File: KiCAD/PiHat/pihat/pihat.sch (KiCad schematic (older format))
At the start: 13 parts, among them J1 Conn_01x03, J2 Conn_01x03, P1 Conn_02x20_Odd_Even, Q1 BSS138, Q2 BSS138

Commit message: compacted servo design
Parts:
- J1, J2: symbol Connector_Generic:Conn_01x03 -> pihat-rescue:Conn_01x03-Connector_Generic
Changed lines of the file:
@@
 EESchema Schematic File Version 4
-LIBS:pihat-cache
 EELAYER 30 0
 EELAYER END
@@
 Connection ~ 7000 3550
 Text GLabel 7450 4450 2    50   Input ~ 0
-GPIO_17
+GPIO_2
 Text Label 8450 3600 2    50   ~ 0
 PAN_SERVO_PIN
@@
 	7000 3550 7450 3550
 Text GLabel 7450 3550 2    50   Input ~ 0
-GPIO_27
+GPIO_3
 Wire Wire Line
 	6050 4450 7450 4450
@@
 GPIO_27
 $Comp
-L Connector_Generic:Conn_01x03 J1
+L pihat-rescue:Conn_01x03-Connector_Generic J1
 U 1 1 5E51AE8D
 P 5300 2550
@@
 Connection ~ 5400 4450
 $Comp
-L Connector_Generic:Conn_01x03 J2
+L pihat-rescue:Conn_01x03-Connector_Generic J2
 U 1 1 5E545433
 P 6250 2550

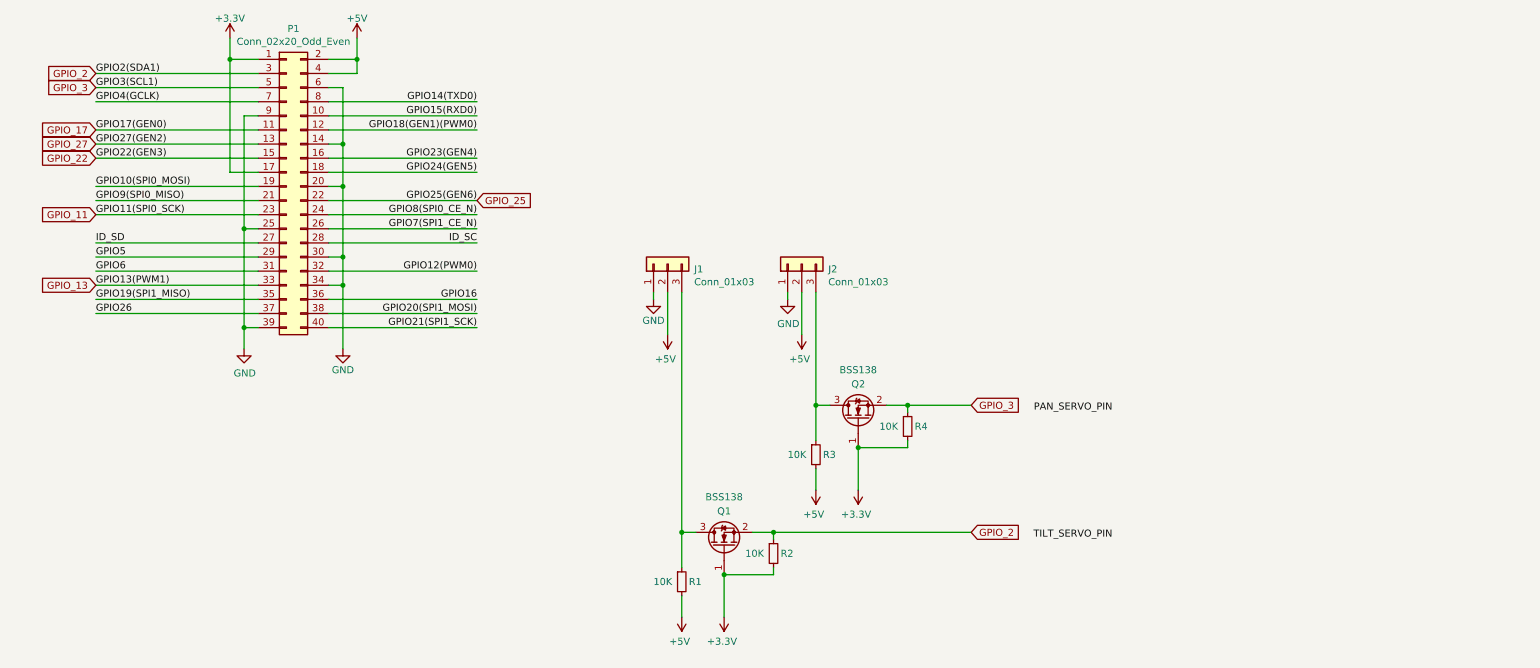
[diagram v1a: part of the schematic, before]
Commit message: Added Fan Header
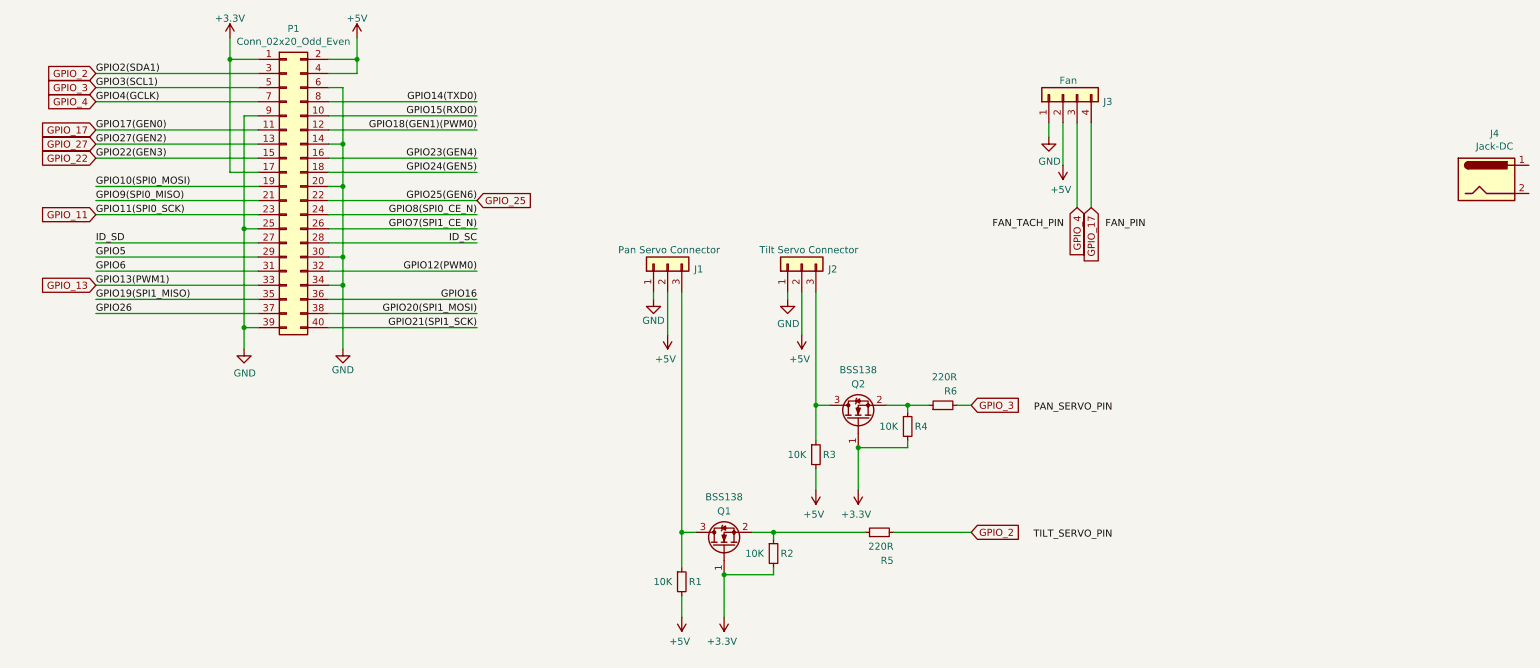
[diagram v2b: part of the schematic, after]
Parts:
- added J3: Fan, Connector_PinHeader_2.54mm:PinHeader_1x04_P2.54mm_Vertical, symbol Connector_Generic:Conn_01x04
- added J4: Jack-DC, symbol Connector:Jack-DC
- added R5, R6: 220R, trailTracer:Yageo_R0805, symbol Device:R_Small
- J1: value Conn_01x03 -> Pan Servo Connector
- J2: value Conn_01x03 -> Tilt Servo Connector
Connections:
- net +5V: now also J3.2 (Pin_2)
- net GND: now also J3.1 (Pin_1)
- net GPIO_17: now also J3.4 (Pin_4)
- net GPIO_2: now also R5.2; no longer Q1.2 (S), R2.1
- net GPIO_3: now also R6.2; no longer Q2.2 (S), R4.1
- net GPIO4(GCLK) renamed GPIO_4
- net GPIO_4: now also J3.3 (Pin_3)
- new net: Q1.2 (S), R2.1, R5.1
- new net: Q2.2 (S), R4.1, R6.1
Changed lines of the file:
@@
 Wire Wire Line
 	2900 2900 3950 2900
-Wire Wire Line
-	6350 2750 6350 3550
 Connection ~ 6650 3850
 Wire Wire Line
@@
 	1    0    0    -1
 $EndComp
-Connection ~ 6350 3550
 Wire Wire Line
 	6350 4150 6350 4000
@@
 Text GLabel 1250 1300 0    50   Input ~ 0
 GPIO_3
-Connection ~ 6050 4450
-Connection ~ 7000 3550
 Text GLabel 7450 4450 2    50   Input ~ 0
 GPIO_2
@@
 Text Label 8450 4500 2    50   ~ 0
 TILT_SERVO_PIN
-Wire Wire Line
-	7000 3550 7450 3550
 Text GLabel 7450 3550 2    50   Input ~ 0
 GPIO_3
-Wire Wire Line
-	6050 4450 7450 4450
 $Comp
 L pihat-rescue:GND-power #PWR03
@@
 P 5300 2550
 F 0 "J1" V 5264 2362 50  0000 R CNN
-F 1 "Conn_01x03" V 5173 2362 50  0000 R CNN
+F 1 "Pan Servo Connector" V 5400 2900 50  0000 R CNN
 F 2 "Connector_PinHeader_2.54mm:PinHeader_1x03_P2.54mm_Vertical" H 5300 2550 50  0001 C CNN
 F 3 "~" H 5300 2550 50  0001 C CNN
@@
 	0    -1   -1   0
 $EndComp
-Wire Wire Line
-	5400 2750 5400 4450
-Connection ~ 5400 4450
 $Comp
 L pihat-rescue:Conn_01x03-Connector_Generic J2
@@
 P 6250 2550
 F 0 "J2" V 6214 2362 50  0000 R CNN
-F 1 "Conn_01x03" V 6123 2362 50  0000 R CNN
+F 1 "Tilt Servo Connector" V 6350 2850 50  0000 R CNN
 F 2 "Connector_PinHeader_2.54mm:PinHeader_1x03_P2.54mm_Vertical" H 6250 2550 50  0001 C CNN
 F 3 "~" H 6250 2550 50  0001 C CNN
@@
 	0    -1   -1   0
 $EndComp
+$Comp
+L Connector:Jack-DC J4
+U 1 1 5E4C915C
+P 11100 1950
+F 0 "J4" H 11157 2275 50  0000 C CNN
+F 1 "Jack-DC" H 11157 2184 50  0000 C CNN
+F 2 "" H 11150 1910 50  0001 C CNN
+F 3 "~" H 11150 1910 50  0001 C CNN
+	1    11100 1950
+	1    0    0    -1
+$EndComp
+$Comp
+L Connector_Generic:Conn_01x04 J3
+U 1 1 5E4CBC36
+P 8100 1350
+F 0 "J3" V 8050 1000 50  0000 L CNN
+F 1 "Fan" V 8200 1250 50  0000 L CNN
+F 2 "Connector_PinHeader_2.54mm:PinHeader_1x04_P2.54mm_Vertical" H 8100 1350 50  0001 C CNN
+F 3 "~" H 8100 1350 50  0001 C CNN
+	1    8100 1350
+	0    -1   -1   0
+$EndComp
+Text GLabel 1250 1400 0    50   Input ~ 0
+GPIO_4
+$Comp
+L power:+5V #PWR07
+U 1 1 5E4D6344
+P 8100 1850
+F 0 "#PWR07" H 8100 1700 50  0001 C CNN
+F 1 "+5V" H 8115 2023 50  0000 C CNN
+F 2 "" H 8100 1850 50  0001 C CNN
+F 3 "" H 8100 1850 50  0001 C CNN
+	1    8100 1850
+	-1   0    0    1
+$EndComp
+Wire Wire Line
+	8000 1550 8000 1650
+Wire Wire Line
+	8100 1550 8100 1850
+Text GLabel 8200 2150 3    50   Input ~ 0
+GPIO_4
+Text GLabel 8300 2150 3    50   Input ~ 0
+GPIO_17
+Wire Wire Line
+	8200 1550 8200 2150
+Text Label 8400 2300 0    50   ~ 0
+FAN_PIN
+Text Label 7600 2300 0    50   ~ 0
+FAN_TACH_PIN
+Wire Wire Line
+	8300 2150 8300 1550
+$Comp
+L power:GND #PWR06
+U 1 1 5E4D5B19
+P 8000 1650
+F 0 "#PWR06" H 8000 1400 50  0001 C CNN
+F 1 "GND" H 8005 1477 50  0000 C CNN
+F 2 "" H 8000 1650 50  0001 C CNN
+F 3 "" H 8000 1650 50  0001 C CNN
+	1    8000 1650
+	1    0    0    -1
+$EndComp
+$Comp
+L Device:R_Small R5
+U 1 1 5E518064
+P 6800 4450
+F 0 "R5" V 6600 4350 50  0000 L CNN
+F 1 "220R" V 6700 4350 50  0000 L CNN
+F 2 "trailTracer:Yageo_R0805" H 6800 4450 50  0001 C CNN
+F 3 "~" H 6800 4450 50  0001 C CNN
+	1    6800 4450
+	0    -1   -1   0
+$EndComp
+Wire Wire Line
+	5400 4450 5400 2750
+Connection ~ 5400 4450
+Wire Wire Line
+	7450 4450 6900 4450
+Wire Wire Line
+	6700 4450 6050 4450
+Connection ~ 6050 4450
+Wire Wire Line
+	6350 3550 6350 2750
+Connection ~ 6350 3550
+$Comp
+L Device:R_Small R6
+U 1 1 5E52C769
+P 7250 3550
+F 0 "R6" V 7350 3450 50  0000 L CNN
+F 1 "220R" V 7450 3450 50  0000 L CNN
+F 2 "trailTracer:Yageo_R0805" H 7250 3550 50  0001 C CNN
+F 3 "~" H 7250 3550 50  0001 C CNN
+	1    7250 3550
+	0    -1   -1   0
+$EndComp
+Wire Wire Line
+	7350 3550 7450 3550
+Wire Wire Line
+	7150 3550 7000 3550
+Connection ~ 7000 3550
 $EndSCHEMATC

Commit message: Temporary Commit
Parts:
- removed J4: Jack-DC, symbol Connector:Jack-DC
- added J4: Power Connector, Connector_JST:JST_VH_S2P-VH_1x02_P3.96mm_Horizontal, symbol Connector_Generic:Conn_01x02
- added U1: TPS5431DDA, Package_SO:TI_SO-PowerPAD-8_ThermalVias, symbol Regulator_Switching:TPS5431DDA
- J3: footprint Connector_PinHeader_2.54mm:PinHeader_1x04_P2.54mm_Vertical -> Connector_PinHeader_2.54mm:PinHeader_1x04_P2.54mm_Horizontal
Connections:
- wire segments 82 -> 84
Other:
- moved on the sheet: J1, J2, J3, MK1, MK2, MK3, MK4, P1, Q1, Q2, R1, R2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

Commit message: Minor commit
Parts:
- J3: footprint Connector_PinHeader_2.54mm:PinHeader_1x04_P2.54mm_Horizontal -> Connector_PinHeader_2.54mm:PinHeader_1x04_P2.54mm_Vertical
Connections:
- net labels added: Pi_Power+, Pi_Power_-
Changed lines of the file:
@@
 EESchema Schematic File Version 4
+LIBS:pihat-cache
 EELAYER 30 0
 EELAYER END
 $Descr A1 33110 23386
 encoding utf-8
-Sheet 1 1
+Sheet 1 2
 Title ""
 Date "15 nov 2012"
@@
 F 0 "J3" V 12350 3750 50  0000 L CNN
 F 1 "Fan" V 12500 4000 50  0000 L CNN
-F 2 "Connector_PinHeader_2.54mm:PinHeader_1x04_P2.54mm_Horizontal" H 12400 4100 50  0001 C CNN
+F 2 "Connector_PinHeader_2.54mm:PinHeader_1x04_P2.54mm_Vertical" H 12400 4100 50  0001 C CNN
 F 3 "~" H 12400 4100 50  0001 C CNN
 	1    12400 4100
@@
 L power:+5V #PWR07
 U 1 1 5E4D6344
-P 12400 4600
-F 0 "#PWR07" H 12400 4450 50  0001 C CNN
-F 1 "+5V" H 12415 4773 50  0000 C CNN
-F 2 "" H 12400 4600 50  0001 C CNN
-F 3 "" H 12400 4600 50  0001 C CNN
-	1    12400 4600
-	-1   0    0    1
-$EndComp
-Wire Wire Line
-	12300 4300 12300 4400
-Wire Wire Line
-	12400 4300 12400 4600
-Text GLabel 12500 4900 3    50   Input ~ 0
+P 12500 4600
+F 0 "#PWR07" H 12500 4450 50  0001 C CNN
+F 1 "+5V" H 12515 4773 50  0000 C CNN
+F 2 "" H 12500 4600 50  0001 C CNN
+F 3 "" H 12500 4600 50  0001 C CNN
+	1    12500 4600
+	-1   0    0    1
+$EndComp
+Wire Wire Line
+	12600 4300 12600 4400
+Wire Wire Line
+	12500 4300 12500 4600
+Text GLabel 12400 4900 3    50   Input ~ 0
 GPIO_4
-Text GLabel 12600 4900 3    50   Input ~ 0
+Text GLabel 12300 4900 3    50   Input ~ 0
 GPIO_17
 Wire Wire Line
-	12500 4300 12500 4900
-Text Label 12700 5050 0    50   ~ 0
+	12400 4300 12400 4900
+Text Label 14650 5500 0    50   ~ 0
 FAN_PIN
-Text Label 11900 5050 0    50   ~ 0
+Text Label 13850 5500 0    50   ~ 0
 FAN_TACH_PIN
 Wire Wire Line
-	12600 4900 12600 4300
+	12300 4900 12300 4300
 $Comp
 L power:GND #PWR06
 U 1 1 5E4D5B19
-P 12300 4400
-F 0 "#PWR06" H 12300 4150 50  0001 C CNN
-F 1 "GND" H 12305 4227 50  0000 C CNN
-F 2 "" H 12300 4400 50  0001 C CNN
-F 3 "" H 12300 4400 50  0001 C CNN
-	1    12300 4400
+P 12600 4400
+F 0 "#PWR06" H 12600 4150 50  0001 C CNN
+F 1 "GND" H 12605 4227 50  0000 C CNN
+F 2 "" H 12600 4400 50  0001 C CNN
+F 3 "" H 12600 4400 50  0001 C CNN
+	1    12600 4400
 	1    0    0    -1
 $EndComp
@@
 L Regulator_Switching:TPS5431DDA U1
 U 1 1 5E503B5A
-P 11600 3200
-F 0 "U1" H 11600 3667 50  0000 C CNN
-F 1 "TPS5431DDA" H 11600 3576 50  0000 C CNN
-F 2 "Package_SO:TI_SO-PowerPAD-8_ThermalVias" H 11650 2850 50  0001 L CIN
-F 3 "http://www.ti.com/lit/ds/symlink/tps5430.pdf" H 11600 3200 50  0001 C CNN
-	1    11600 3200
-	1    0    0    -1
-$EndComp
+P 12250 2600
+F 0 "U1" H 12250 3067 50  0000 C CNN
+F 1 "TPS5431DDA" H 12250 2976 50  0000 C CNN
+F 2 "Package_SO:TI_SO-PowerPAD-8_ThermalVias" H 12300 2250 50  0001 L CIN
+F 3 "http://www.ti.com/lit/ds/symlink/tps5430.pdf" H 12250 2600 50  0001 C CNN
+	1    12250 2600
+	1    0    0    -1
+$EndComp
+$Sheet
+S 20050 2950 5850 4000
+U 5E5833CB
+F0 "Power_Sheet" 50
+F1 "Power.sch" 50
+$EndSheet
+Text GLabel 13700 4000 1    50   Input ~ 0
+Pi_Power+
+Text GLabel 13800 4000 1    50   Input ~ 0
+Pi_Power_-
 $EndSCHEMATC

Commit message: Added status LEDs, power relay, organized traces
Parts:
- removed U1: TPS5431DDA, Package_SO:TI_SO-PowerPAD-8_ThermalVias, symbol Regulator_Switching:TPS5431DDA
- added C1: 100 uF, Resistor_SMD:R_1206_3216Metric, symbol Device:C_Small
- added C2: 10 nF, Resistor_SMD:R_1206_3216Metric, symbol Device:C_Small
- added C3: 270 uF, Capacitor_THT:CP_Radial_D10.0mm_P5.00mm, symbol Device:CP1_Small
- added C4: 10nF, Resistor_SMD:R_1206_3216Metric_Pad1.42x1.75mm_HandSolder, symbol Device:C_Small
- added C5: 220 uF, Capacitor_SMD:C_1206_3216Metric_Pad1.42x1.75mm_HandSolder, symbol Device:C_Small
- added D1: B340, trailTracer:DO-214, symbol Diode:B340
- added D2: 1N4001, Diode_THT:D_DO-41_SOD81_P10.16mm_Horizontal, symbol Diode:1N4001
- added D3, D4: LED, LED_THT:LED_D3.0mm, symbol Device:LED
- added L1: 15 uH, trailTracer:Coil, symbol Device:L
- added P2, P3, P4, P5, P6, P7: Pad, trailTracer:Pad, symbol trailTracer:Pad
- added R10, R12: R_Small, Resistor_SMD:R_0805_2012Metric_Pad1.15x1.40mm_HandSolder, symbol Device:R_Small
- added R11: 10K, Resistor_SMD:R_0805_2012Metric, symbol Device:R_Small
- added R7: 10 KOhm, Resistor_SMD:R_0805_2012Metric, symbol Device:R_Small
- added R8: 3.24 KOhm, Resistor_SMD:R_0805_2012Metric, symbol Device:R_Small
- added R9: 15K, Resistor_SMD:R_0805_2012Metric, symbol Device:R_Small
- added U1: TPS5430-Q1, Package_SO:SOIC-8-1EP_3.9x4.9mm_P1.27mm_EP2.41x3.81mm_ThermalVias, symbol trailTracer:TPS5430-Q1
- added U2: TMP36xS, Package_SO:SOIC-8_3.9x4.9mm_P1.27mm, symbol Sensor_Temperature:TMP36xS
- added U3: ATTiny85, Package_DIP:DIP-8_W7.62mm, symbol trailTracer:ATTiny85
- added U4: TE_OJ-SH-105LM, trailTracer:TE_OJ-SH-105LM, symbol trailTracer:TE_OJ-SH-105LM
- R1, R2, R3, R4, R5, R6: footprint trailTracer:Yageo_R0805 -> Resistor_SMD:R_0805_2012Metric
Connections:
- net labels added: PI_5V
- wire segments 84 -> 157
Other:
- note added: "P7: Jump to ATTiny85 output pad.\n"
- moved on the sheet: J4

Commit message: Peer review changes
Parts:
- R10: value R_Small -> 470
- R12: value R_Small -> 120R
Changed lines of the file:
@@
 EESchema Schematic File Version 4
+LIBS:pihat-cache
 EELAYER 30 0
 EELAYER END
@@
 Pi_Power+
 Text GLabel 13800 4000 1    50   Input ~ 0
-Pi_Power_-
-Text GLabel 13700 4000 1    50   Input ~ 0
 Pi_Power+
 Wire Wire Line
@@
 P 14200 4300
 F 0 "R10" V 14300 4150 50  0000 C CNN
-F 1 "R_Small" V 14300 4400 50  0000 C CNN
+F 1 "470" V 14300 4400 50  0000 C CNN
 F 2 "Resistor_SMD:R_0805_2012Metric_Pad1.15x1.40mm_HandSolder" H 14200 4300 50  0001 C CNN
 F 3 "~" H 14200 4300 50  0001 C CNN
@@
 P 12800 9900
 F 0 "R12" V 12900 9750 50  0000 C CNN
-F 1 "R_Small" V 12900 10000 50  0000 C CNN
+F 1 "120R" V 12900 10000 50  0000 C CNN
 F 2 "Resistor_SMD:R_0805_2012Metric_Pad1.15x1.40mm_HandSolder" H 12800 9900 50  0001 C CNN
 F 3 "~" H 12800 9900 50  0001 C CNN
